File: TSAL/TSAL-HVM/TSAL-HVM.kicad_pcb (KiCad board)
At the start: 2 copper layers, 80.9 x 57.8 mm, 41 parts, among them J1 HV+, J2 HV-, J3 Conn_01x03_Male, J4 VHI, K1 TE_PCH-1xxx2M, Q1 2N7002, Q2 2N7002, Q3 2N7002, U1 SPAN02A-12, U2 LM311

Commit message: update TSAL PCB v1.1
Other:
- board text added: "Board to be conformal coated"
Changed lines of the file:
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@@
   (general
     (thickness 1.6)
-    (drawings 27)
+    (drawings 29)
     (tracks 177)
     (zones 0)
@@
     )
   )
+  (gr_text "Board to be conformal coated" (at 102.235 104.14) (layer Eco1.User)
+    (effects (font (size 1 1) (thickness 0.15)))
+  )
+  (dimension 7.62 (width 0.12) (layer Eco1.User)
+    (gr_text "7.620 mm" (at 101.6 102.87) (layer Eco1.User)
+      (effects (font (size 1 1) (thickness 0.15)))
+    )
+    (feature1 (pts (xy 105.41 93.98) (xy 105.41 102.186421)))
+    (feature2 (pts (xy 97.79 93.98) (xy 97.79 102.186421)))
+    (crossbar (pts (xy 97.79 101.6) (xy 105.41 101.6)))
+    (arrow1a (pts (xy 105.41 101.6) (xy 104.283496 102.186421)))
+    (arrow1b (pts (xy 105.41 101.6) (xy 104.283496 101.013579)))
+    (arrow2a (pts (xy 97.79 101.6) (xy 98.916504 102.186421)))
+    (arrow2b (pts (xy 97.79 101.6) (xy 98.916504 101.013579)))
+  )
   (gr_line (start 102.235 88.9) (end 106.68 88.9) (layer F.SilkS) (width 1))

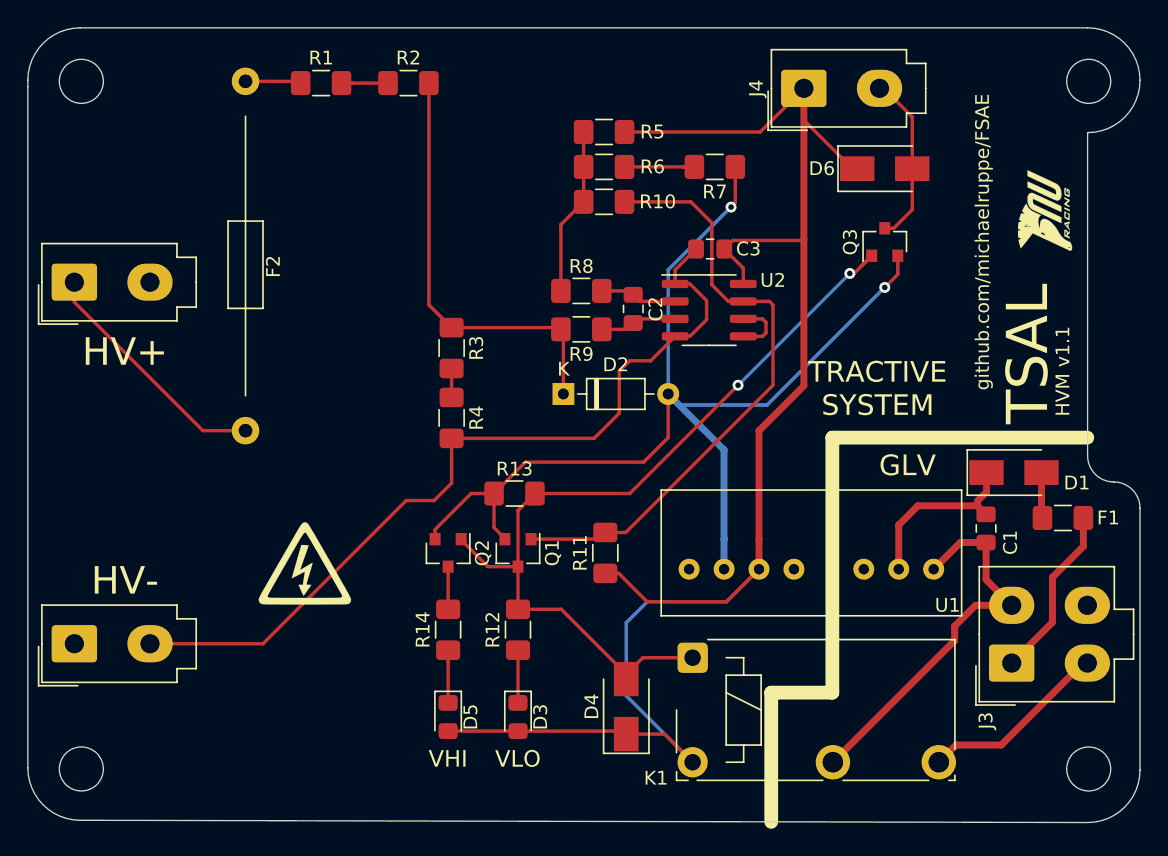
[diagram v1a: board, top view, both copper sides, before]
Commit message: Update TSAL to v2. Add AIL
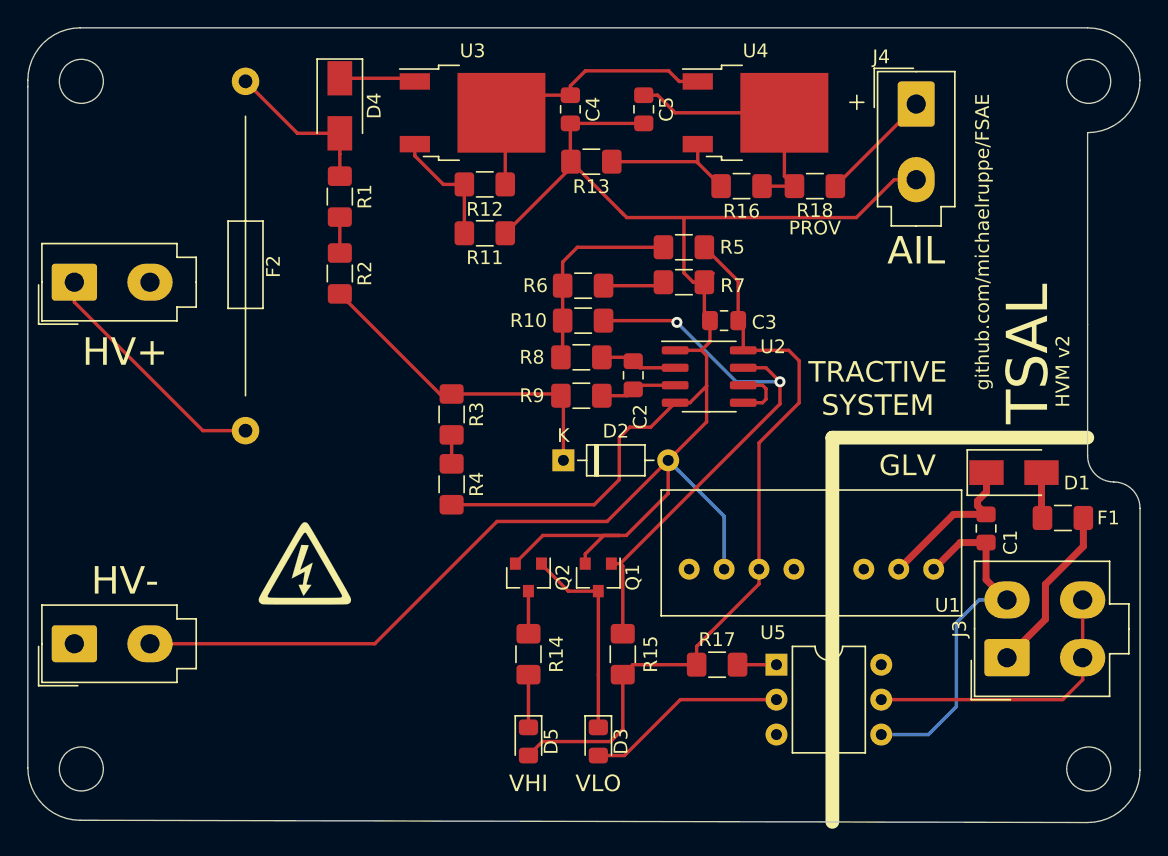
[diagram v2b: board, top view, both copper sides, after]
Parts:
- removed D6: D, Diode_SMD:D_SMA
- removed the G*** at (122.2, 53.8)
- removed K1: TE_PCH-1xxx2M, Relay_THT:Relay_SPST_TE_PCH-1xxx2M
- removed Q3: 2N7002, Package_TO_SOT_SMD:SOT-23
- added C4: 1u, Capacitor_SMD:C_0805_2012Metric_Pad1.15x1.40mm_HandSolder, F.Cu at (87.6, 46.5)
- added C5: 1u, Capacitor_SMD:C_0805_2012Metric_Pad1.15x1.40mm_HandSolder, F.Cu at (93.0, 46.5)
- added R15: 10k, Resistor_SMD:R_1206_3216Metric_Pad1.42x1.75mm_HandSolder, F.Cu at (91.4, 86.1)
- added R16: 6k04, Resistor_SMD:R_1206_3216Metric_Pad1.42x1.75mm_HandSolder, F.Cu at (100.1, 52.1)
- added R17: 2k2, Resistor_SMD:R_1206_3216Metric_Pad1.42x1.75mm_HandSolder, F.Cu at (98.3, 86.9)
- added R18: PROV, Resistor_SMD:R_1206_3216Metric_Pad1.42x1.75mm_HandSolder, F.Cu at (105.4, 52.1)
- added U3: LR8K4-G, Package_TO_SOT_SMD:TO-252-2, F.Cu at (80.5, 46.7)
- added U4: LR8K4-G, Package_TO_SOT_SMD:TO-252-2, F.Cu at (101.1, 46.7)
- added U5: 8021, Package_DIP:DIP-6_W7.62mm, F.Cu at (102.6, 86.9)
- J3: value Conn_01x03_Male -> Conn_01x04_Male
- J4: value VHI -> AIL
- R11: value 24k -> 202k
- R12: value 2k2 -> 6k04
- R13: value 24k -> 47k
- R14: value 2k2 -> 3k3
- moved D4 48.4 mm to (70.9, 46.2), turned to 270 degrees
- moved R12 32.5 mm to (81.4, 51.9), turned to 180 degrees
- moved R11 24.8 mm to (81.4, 55.5), turned to 0 degrees
- moved R13 24.8 mm to (89.2, 50.3)
- moved R2 14.7 mm to (70.9, 58.4), turned to 270 degrees
- moved R5 10.2 mm to (95.9, 56.5)
- moved R10 8.77 mm to (88.6, 61.8)
- moved R6 8.77 mm to (88.6, 59.3)
- moved R7 8.68 mm to (95.9, 59.1)
- moved R1 8.37 mm to (70.9, 52.8), turned to 270 degrees
- moved J4 8.25 mm to (112.8, 46.1), turned to 0 degrees
- moved D3 6.11 mm to (89.7, 92.4)
- moved Q1 6.11 mm to (89.7, 80.5)
- moved D5 6.11 mm to (84.6, 92.4)
- moved Q2 6.11 mm to (84.6, 80.5)
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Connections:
- net +Vin renamed Net-(F1-Pad1)
- net Net-(D2-Pad1) renamed /Vin
- net Net-(R10-Pad1) renamed /Vref
- D3 pad 2: +12V -> Net-(D3-Pad2)
- D4 pad 1: +12V -> Net-(D4-Pad1)
- F2 pad 2: Net-(F2-Pad2) -> Net-(D4-Pad2)
- J3 pad 3: OUT -> VHI
- J3 pad 4: (no net) -> VHI
- J4 pad 1: +12V -> Net-(J4-Pad1)
- J4 pad 2: Net-(D6-Pad2) -> GND
- Q1 pad 3: Net-(D4-Pad2) -> Net-(D3-Pad1)
- Q2 pad 1: Net-(D4-Pad2) -> Net-(D3-Pad1)
- R1 pad 1: Net-(F2-Pad2) -> Net-(D4-Pad2)
- R11 pad 1: +12V -> Net-(R11-Pad1)
- R11 pad 2: Net-(Q1-Pad1) -> GND
- R12 pad 1: Net-(D3-Pad1) -> Net-(C4-Pad1)
- R12 pad 2: Net-(D4-Pad2) -> Net-(R11-Pad1)
- R13 pad 1: Net-(D4-Pad2) -> Net-(R13-Pad1)
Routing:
- net +12V: track 122.7 -> 55.3 mm
- net Net-(D4-Pad2): track 62.2 -> 11.5 mm, vias 2 -> 0
- net VHI: track 0.00 -> 21.6 mm
- net Net-(C4-Pad1): track 0.00 -> 21.6 mm
- net GND: track 143.8 -> 164.0 mm, vias 2 -> 0
- net Net-(C5-Pad1): track 0.00 -> 19.1 mm
- net Net-(D3-Pad2): track 0.00 -> 14.6 mm
- net OUT: track 13.8 -> 0.00 mm
- net Net-(D6-Pad2): track 12.5 -> 0.00 mm
- net Net-(D3-Pad1): track 3.83 -> 14.9 mm
- net Net-(R13-Pad1): track 0.00 -> 10.0 mm
- net Net-(R11-Pad1): track 0.00 -> 9.11 mm
- net Net-(J4-Pad1): track 0.00 -> 8.40 mm
- net /Vin: track 31.2 -> 23.9 mm
- net Net-(D4-Pad1): track 0.00 -> 5.55 mm
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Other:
- board text added: "DON'T PANIC"
- board text added: "HVM v2"
- board text removed: "Board to be conformal coated"
- board text removed: "HVM v1.1"

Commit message: Update TSAL with connector 3D models
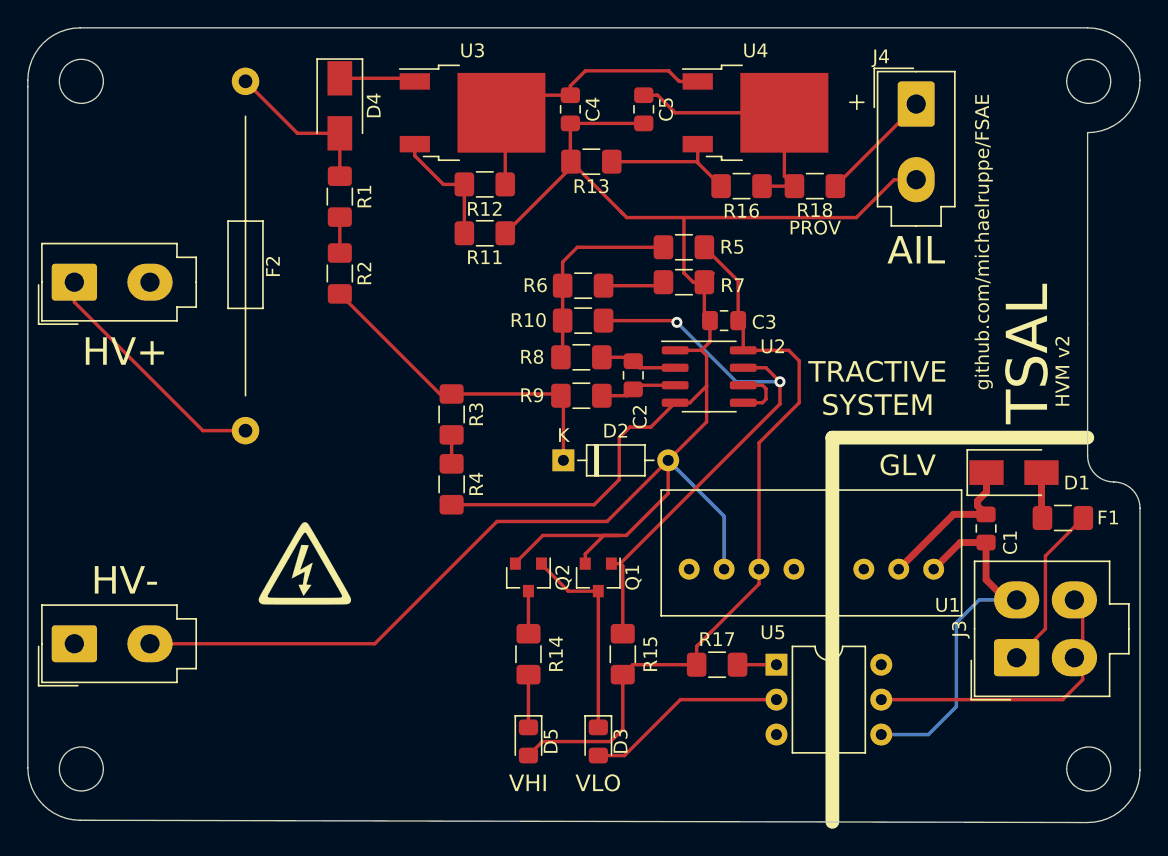
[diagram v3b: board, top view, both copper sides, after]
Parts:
- J3: footprint Connector_Molex:Molex_Mini-Fit_Jr_5566-04A_2x02_P4.20mm_Vertical -> MOLEX-MiniFitJr-4.2mm:Molex-Mini-Fit-Jr-4-pin-P4.2mm-RowP4.2mm

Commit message: Update to v2.1
cosmetic changes to silkscreen. Remove power input fuse
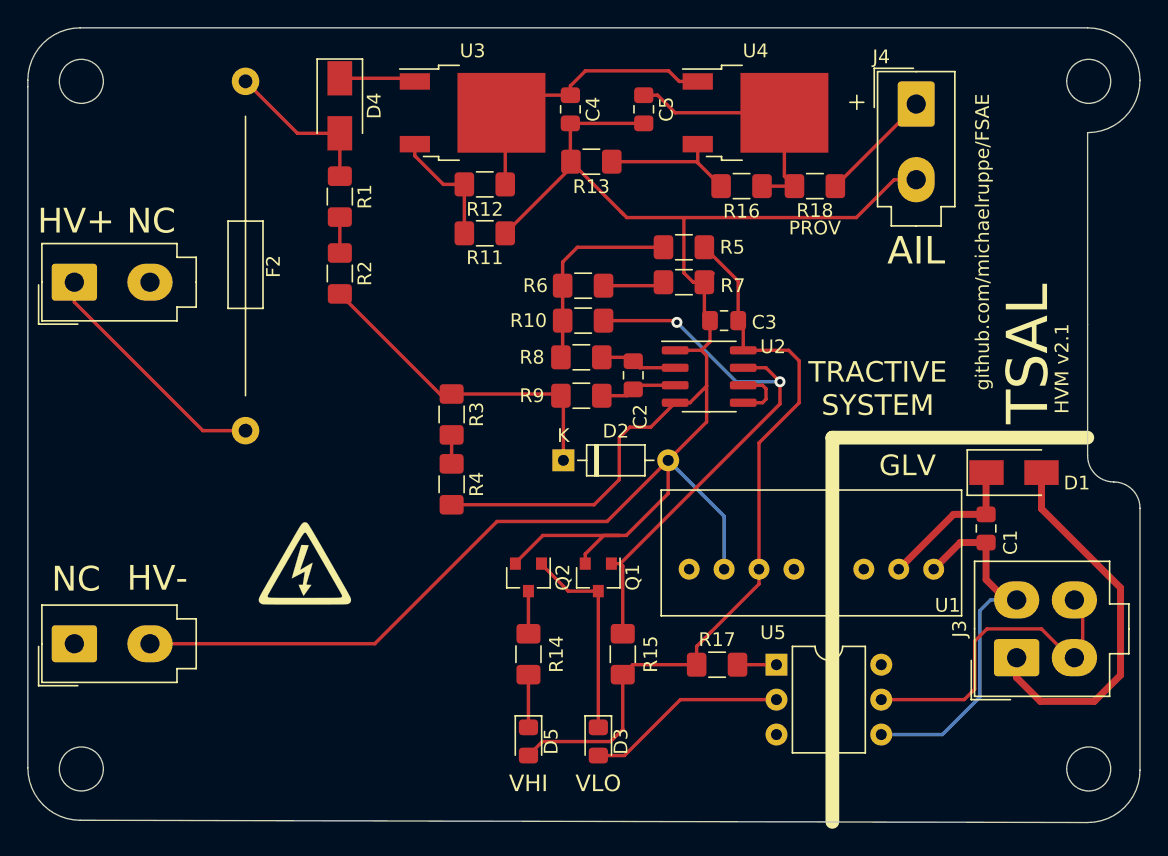
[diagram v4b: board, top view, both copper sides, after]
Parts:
- removed F1: Fuse_Small, Fuse:Fuse_1206_3216Metric_Pad1.42x1.75mm_HandSolder
- U5: value 8021 -> MOC8021
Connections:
- J1 pad 2: Net-(J1-Pad2) -> (no net)
- J2 pad 1: Net-(J2-Pad1) -> (no net)
- J3 pad 1: Net-(F1-Pad1) -> Net-(D1-Pad2)
- U1 pad 3: Net-(U1-Pad3) -> (no net)
- U1 pad 5: Net-(U1-Pad5) -> (no net)
- U1 pad 8: Net-(U1-Pad8) -> (no net)
- U5 pad 3: Net-(U5-Pad3) -> (no net)
- U5 pad 6: Net-(U5-Pad6) -> (no net)
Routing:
- net Net-(D1-Pad2): track 3.33 -> 27.6 mm
- net Net-(F1-Pad1): track 12.2 -> 0.00 mm
- net VHI: track 21.6 -> 23.9 mm
- net -Vin: track 27.1 -> 27.9 mm
- net Net-(C1-Pad2): track 11.6 -> 11.1 mm
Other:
- board text added: "HVM v2.1"
- board text added: "NC"
- board text removed: "HVM v2"

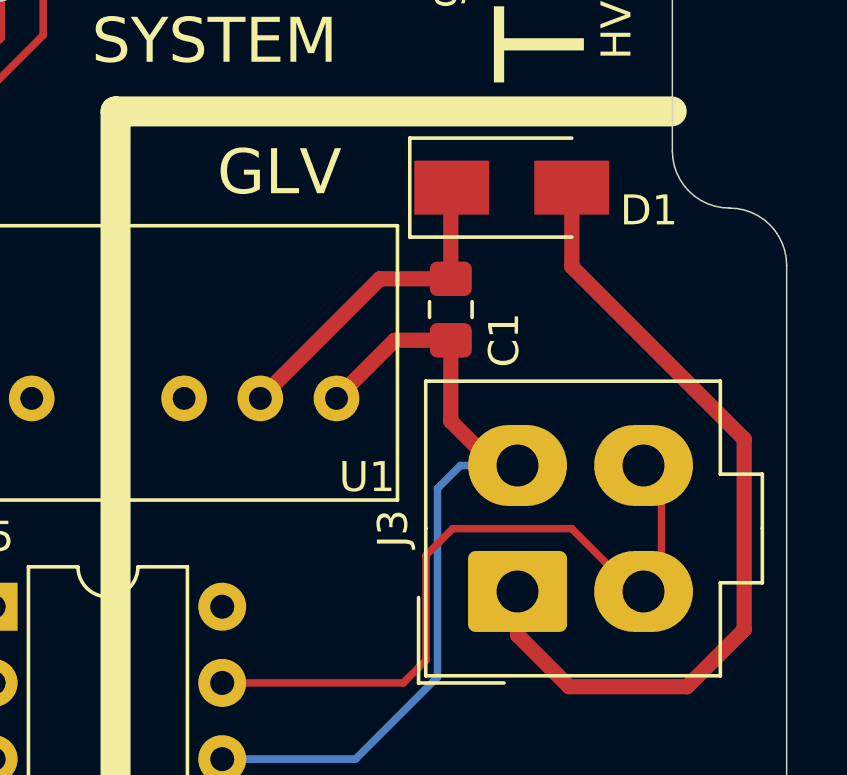
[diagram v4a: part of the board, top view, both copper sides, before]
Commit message: Update net labels and minor power routing in v2.1
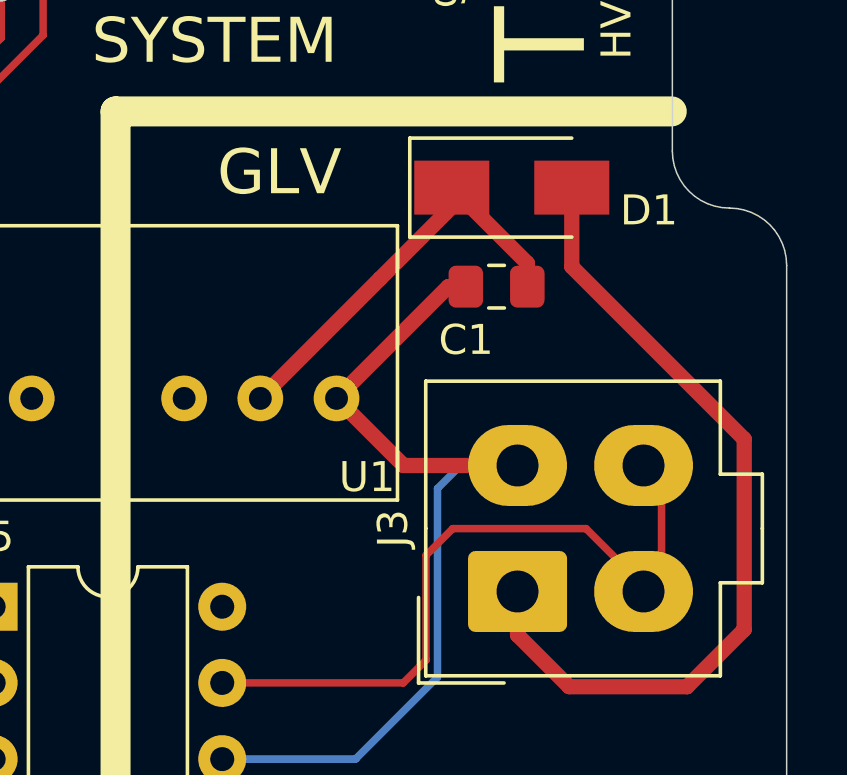
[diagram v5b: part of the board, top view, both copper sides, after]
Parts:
- moved C1 1.70 mm to (119.4, 76.2), turned to 0 degrees
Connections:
- net -Vin renamed GNDPWR
- net VHI renamed /VHI
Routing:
- net Net-(C1-Pad2): track 11.1 -> 14.1 mm
- net GNDPWR: track 27.9 -> 30.4 mm
